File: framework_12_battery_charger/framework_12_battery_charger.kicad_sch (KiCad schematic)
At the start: 1 part, among them IC1 ISL9241HRTZ

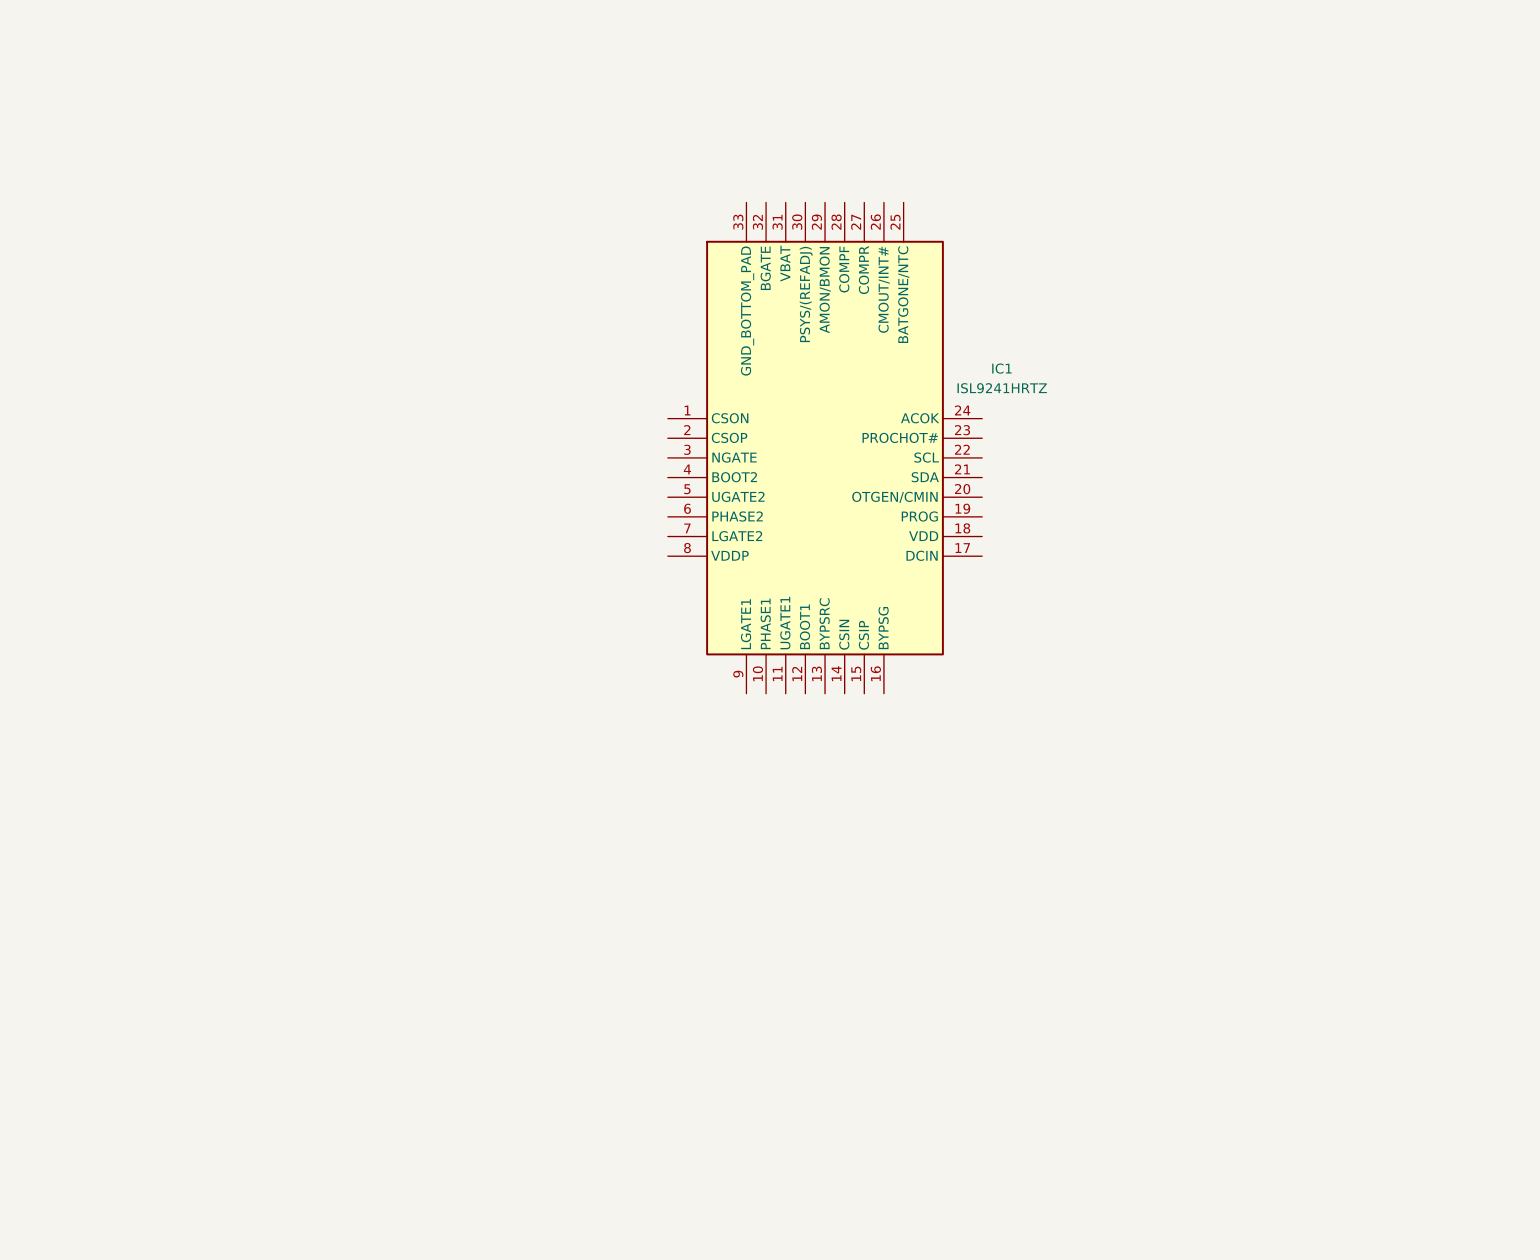
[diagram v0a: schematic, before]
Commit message: Initial schematic based on ils9241 datasheet. still need to select specific resistors and other components, everything's generic rn
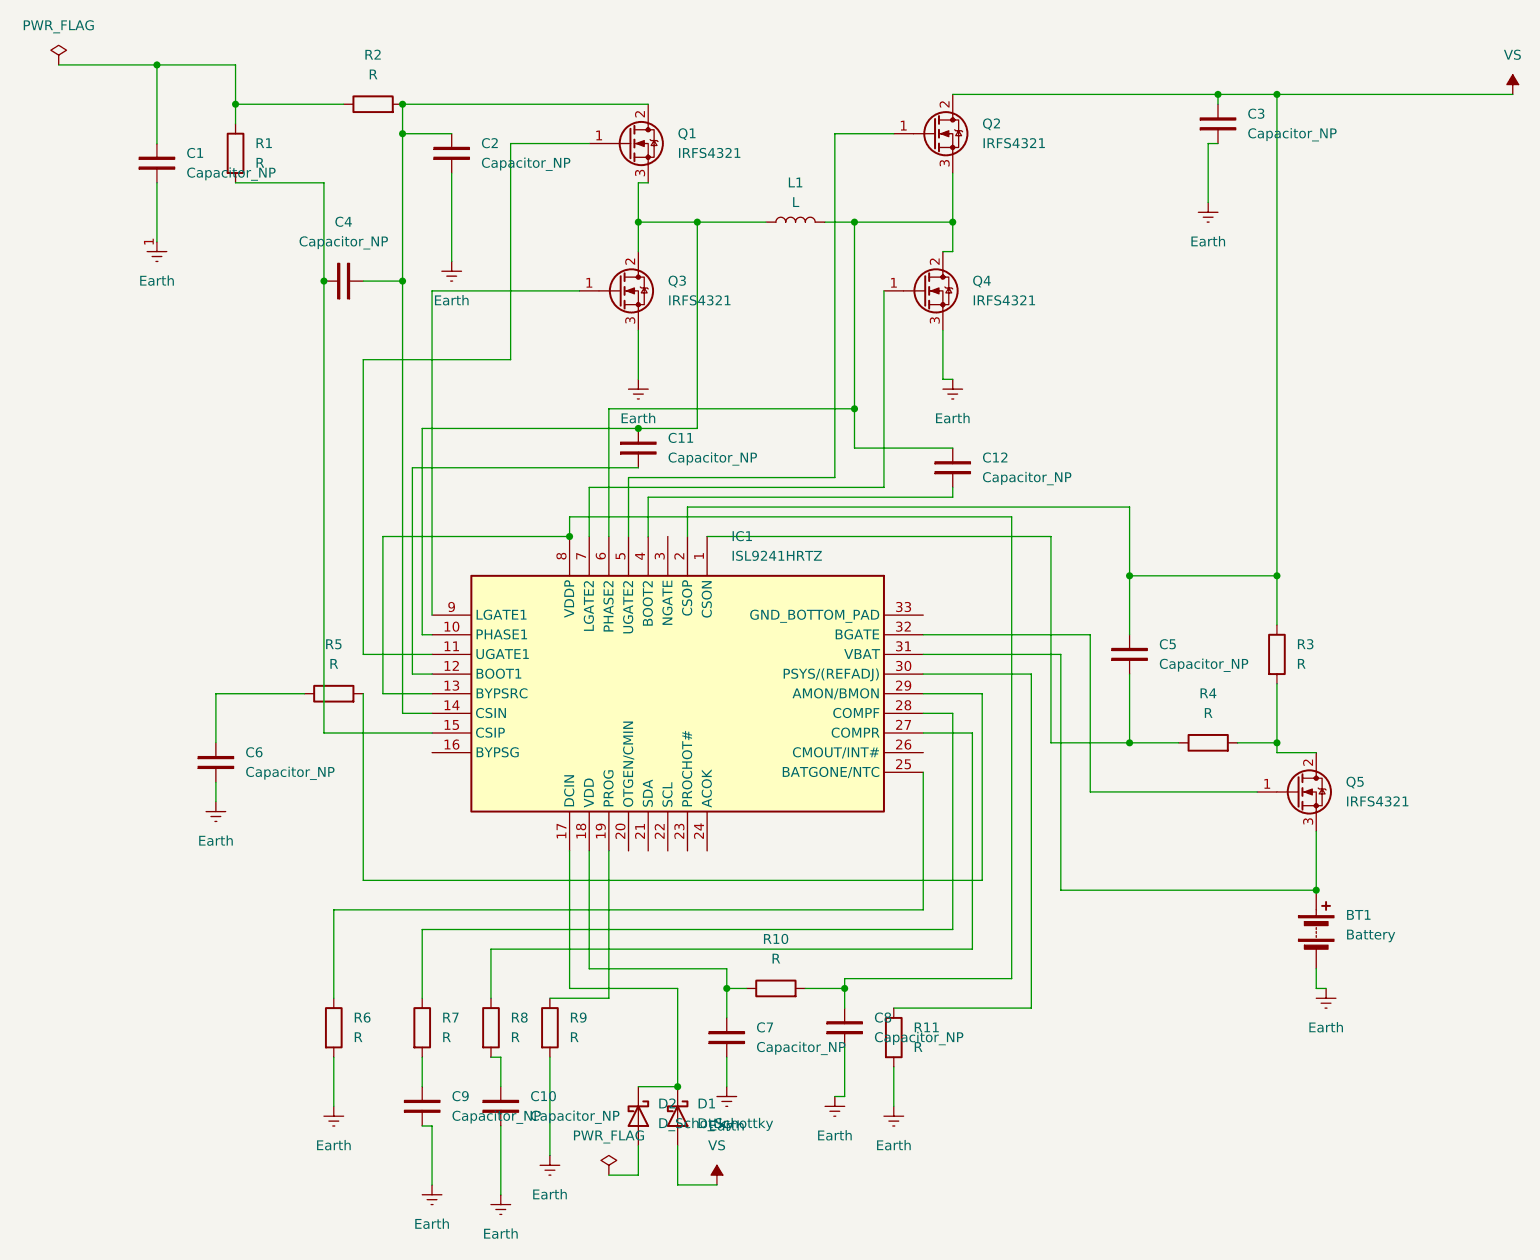
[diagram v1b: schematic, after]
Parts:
- added BT1: Battery, symbol Device:Battery
- added C1, C10, C11, C12, C2, C3, C4, C5, C6, C7, C8, C9: Capacitor_NP, Capacitor_THT:C_Disc_D3.0mm_W2.0mm_P2.50mm, symbol PCM_SL_Devices:Capacitor_NP
- added D1, D2: D_Schottky, symbol Device:D_Schottky
- added L1: L, symbol Device:L
- added Q1, Q2, Q3, Q4, Q5: IRFS4321, Package_TO_SOT_SMD:TO-263-2, symbol Transistor_FET:IRFS4321
- added R1, R10, R11, R2, R3, R4, R5, R6, R7, R8, R9: R, symbol Device:R
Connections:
- net at IC1.1 (CSON): now also C5.1, R4.1
- net at IC1.10 (PHASE1): now also C11.2, L1.1, Q1.3 (S), Q3.2 (D)
- net at IC1.11 (UGATE1): now also Q1.1 (G)
- net at IC1.12 (BOOT1): now also C11.1
- net at IC1.13 (BYPSRC): now also IC1.8 (VDDP), C8.2, R10.2
- net at IC1.14 (CSIN): now also C2.2, C4.1, Q1.2 (D), R2.2
- net at IC1.15 (CSIP): now also C4.2, R1.2
- net at IC1.17 (DCIN): now also D1.1 (K), D2.1 (K)
- net at IC1.18 (VDD): now also C7.2, R10.1
- net at IC1.19 (PROG): now also R9.1
- net VS: now reaches IC1.2 (CSOP)
- net VS: now also C3.2, C5.2, D1.2 (A), Q2.2 (D), R3.1
- net at IC1.25 (BATGONE/NTC): now also R6.1
- net at IC1.27 (COMPR): now also R8.1
- net at IC1.28 (COMPF): now also R7.1
- net at IC1.29 (AMON/BMON): now also R5.2
- net at IC1.30 (PSYS/(REFADJ)): now also R11.1
- net at IC1.31 (VBAT): now also BT1.1 (+), Q5.3 (S)
- net at IC1.32 (BGATE): now also Q5.1 (G)
- net at IC1.4 (BOOT2): now also C12.1
- net at IC1.5 (UGATE2): now also Q2.1 (G)
- net at IC1.6 (PHASE2): now also C12.2, L1.2, Q2.3 (S), Q4.2 (D)
- net at IC1.7 (LGATE2): now also Q4.1 (G)
- net at IC1.9 (LGATE1): now also Q3.1 (G)
- new net: C9.2, R7.2
- new net: C10.2, R8.2
- new net: C1.2, R1.1, R2.1
- new net: Q5.2 (D), R3.2, R4.2
- new net: C6.2, R5.1
- new net Earth: BT1.2 (-), C1.1, C10.1, C2.1, C3.1, C6.1, C7.1, C8.1, C9.1, Q3.3 (S), Q4.3 (S), R11.2, R6.2, R9.2
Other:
- moved on the sheet: IC1

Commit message: Use wire labels
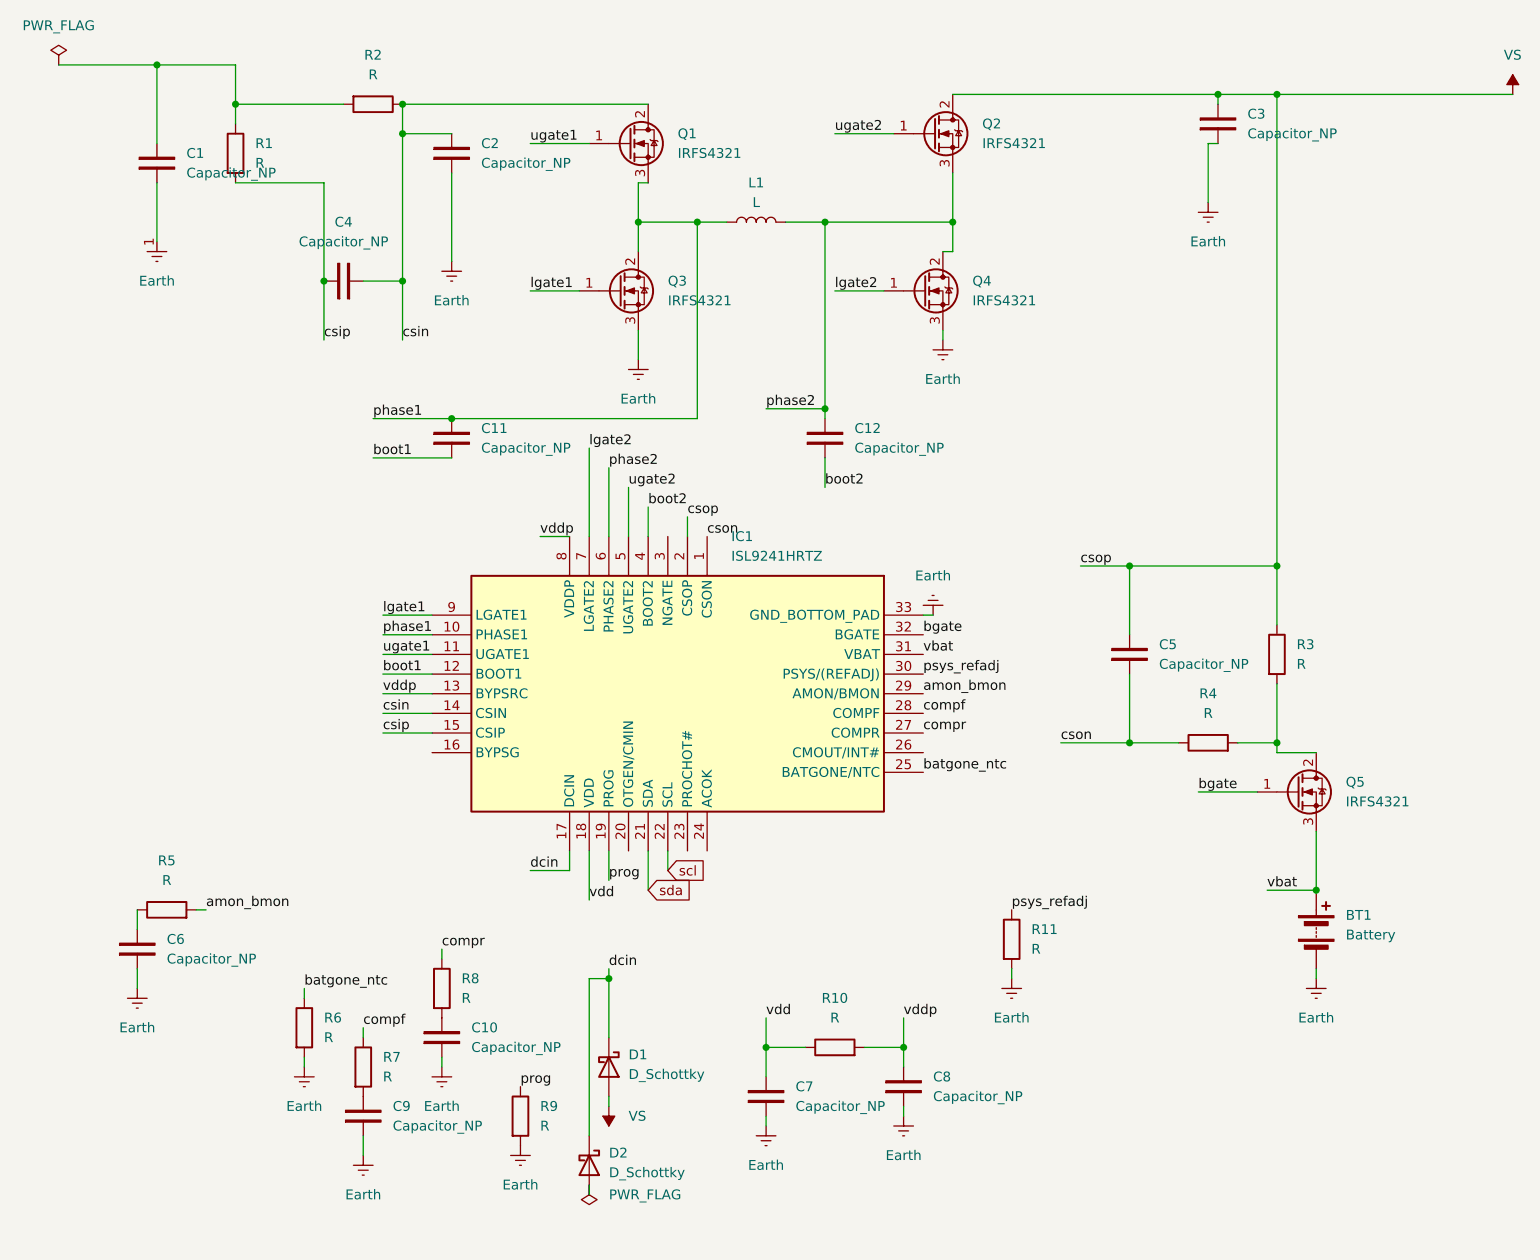
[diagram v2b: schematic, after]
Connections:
- net Earth: now also IC1.33 (GND_BOTTOM_PAD)
- net boot1: now reaches C11.1, IC1.12 (BOOT1)
- net phase1: now reaches C11.2, IC1.10 (PHASE1), L1.1, Q1.3 (S), Q3.2 (D)
- net vddp: now reaches C8.2, IC1.13 (BYPSRC), IC1.8 (VDDP), R10.2
- net csin: now reaches C2.2, C4.1, IC1.14 (CSIN), Q1.2 (D)
- net csin: now also R2.1; no longer R2.2
- net csip: now reaches C4.2, IC1.15 (CSIP), R1.2
- net lgate2: now reaches IC1.7 (LGATE2), Q4.1 (G)
- net phase2: now reaches C12.2, IC1.6 (PHASE2), L1.2, Q2.3 (S), Q4.2 (D)
- net psys_refadj: now reaches IC1.30 (PSYS/(REFADJ)), R11.1
- net dcin: now reaches D1.1 (K), D2.1 (K), IC1.17 (DCIN)
- net prog: now reaches IC1.19 (PROG), R9.1
- net cson: now reaches C5.1, IC1.1 (CSON), R4.1
- net ugate1: now reaches IC1.11 (UGATE1), Q1.1 (G)
- net vdd: now reaches C7.2, IC1.18 (VDD), R10.1
- net sda: now reaches IC1.21 (SDA)
- net scl: now reaches IC1.22 (SCL)
- net batgone_ntc: now reaches IC1.25 (BATGONE/NTC), R6.1
- net compr: now reaches IC1.27 (COMPR), R8.1
- net compf: now reaches IC1.28 (COMPF), R7.1
- net amon_bmon: now reaches IC1.29 (AMON/BMON), R5.2
- net vbat: now reaches BT1.1 (+), IC1.31 (VBAT), Q5.3 (S)
- net bgate: now reaches IC1.32 (BGATE), Q5.1 (G)
- net boot2: now reaches C12.1, IC1.4 (BOOT2)
- net ugate2: now reaches IC1.5 (UGATE2), Q2.1 (G)
- net lgate1: now reaches IC1.9 (LGATE1), Q3.1 (G)
- net at C1.2, R1.1: now also R2.2; no longer R2.1
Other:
- moved on the sheet: C10, C11, C12, C6, C7, C8, C9, D1, D2, L1, R10, R11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
